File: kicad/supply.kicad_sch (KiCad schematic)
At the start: 53 parts, among them J5 Screw_Terminal_01x02, U14 TMUX6123, U17 TMUX6123, U19 L7815, U23 L7915, U6 LM2937-5, U9 LM317_TO-252

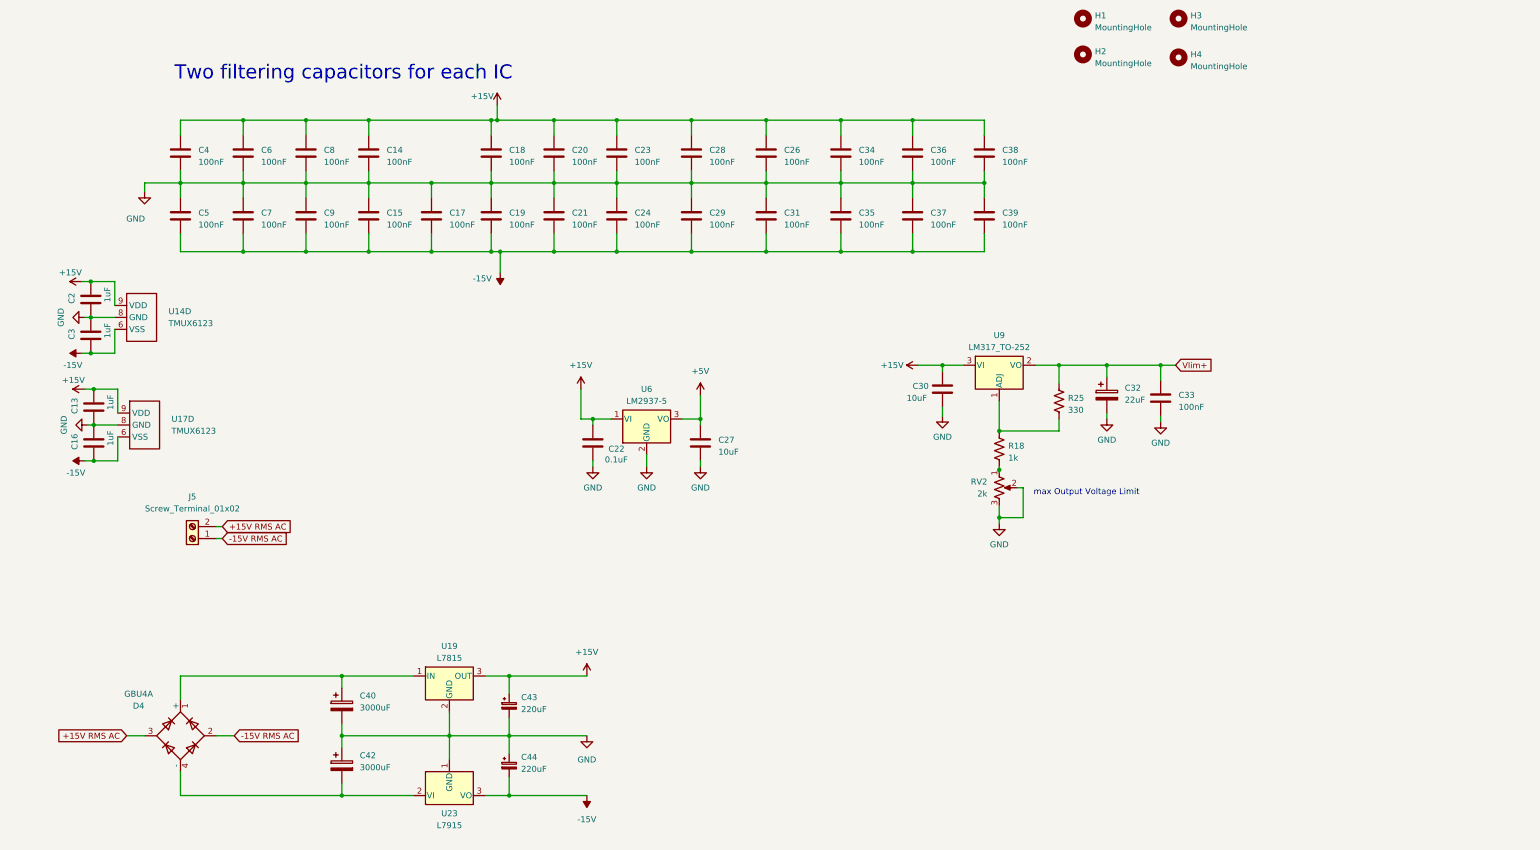
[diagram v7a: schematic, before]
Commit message: Fixed LED Threshold schematic, added second power input screw terminal, first attempt at final placement and routing
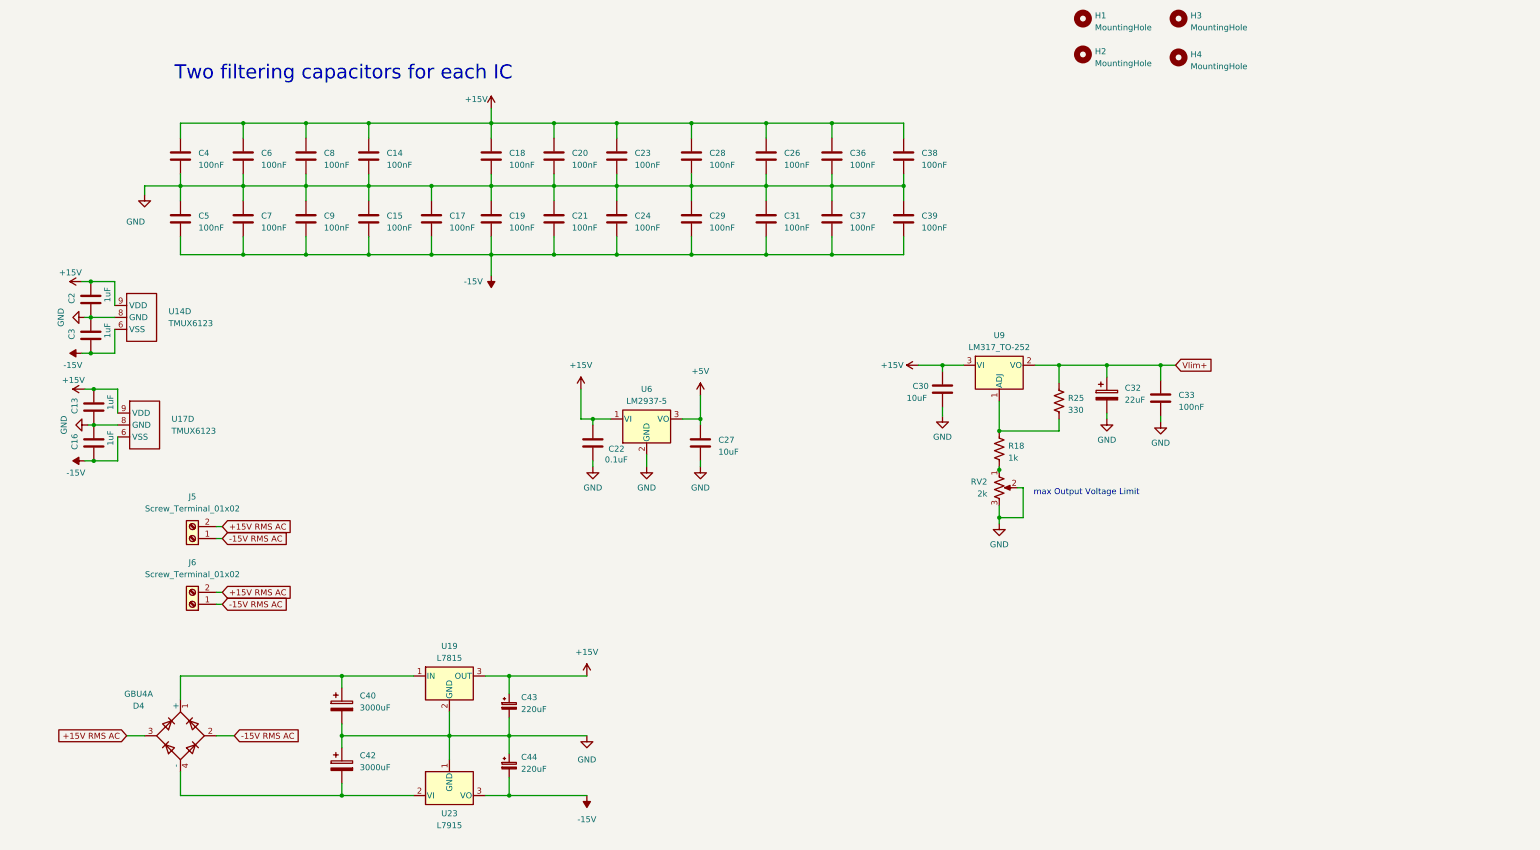
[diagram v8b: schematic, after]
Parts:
- removed C34, C35: 100nF, Capacitor_SMD:C_0805_2012Metric, symbol Device:C
- added J6: Screw_Terminal_01x02, TerminalBlock_4Ucon:TerminalBlock_4Ucon_1x02_P3.50mm_Horizontal, symbol Connector:Screw_Terminal_01x02
- C40, C42: DIGIKEY (none) -> P122523CT-ND; DIGIKEY PARTNO P122523CT-ND -> (none); MPN EEE-FK1V302SV -> (none); PARTNO (none) -> EEE-FK1V302SV
- C43, C44: DIGIKEY (none) -> PCE3812CT-ND; DIGIKEY PARTNO PCE3812CT-ND -> (none); MPN EEE-FK1H221P -> (none); PARTNO (none) -> EEE-FK1H221P
- D4: DIGIKEY (none) -> GBU4A-ND; DIGIKEY PARTNO GBU4A-ND -> (none); MPN GBU4A -> (none); PARTNO (none) -> GBU4A
- RV2: DIGIKEY (none) -> 118-PV36W202C01B00-ND; PARTNO (none) -> PV36W202C01B00
- U6: DIGIKEY (none) -> LM2937ESX-3.3/NOPB; PARTNO (none) -> LM2937ESX-3.3/NOPB
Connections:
- net +15V RMS AC: now also J6.2 (Pin_2)
- net -15V RMS AC: now also J6.1 (Pin_1)
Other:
- moved on the sheet: C14, C15, C17, C18, C19, C20, C21, C23, C24, C26, C28, C29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
